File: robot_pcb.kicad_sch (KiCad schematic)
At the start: 112 parts, among them J1 Raspberry_Pi_2_3, J10 Servo_TrayRelease, J14 Motor FR, J16 19V Output, J17 Programmer, J2 Power_Bypass, J23 Motor BR, J25 ConductClaw, J26 Motor BL, J27 TOF_Front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

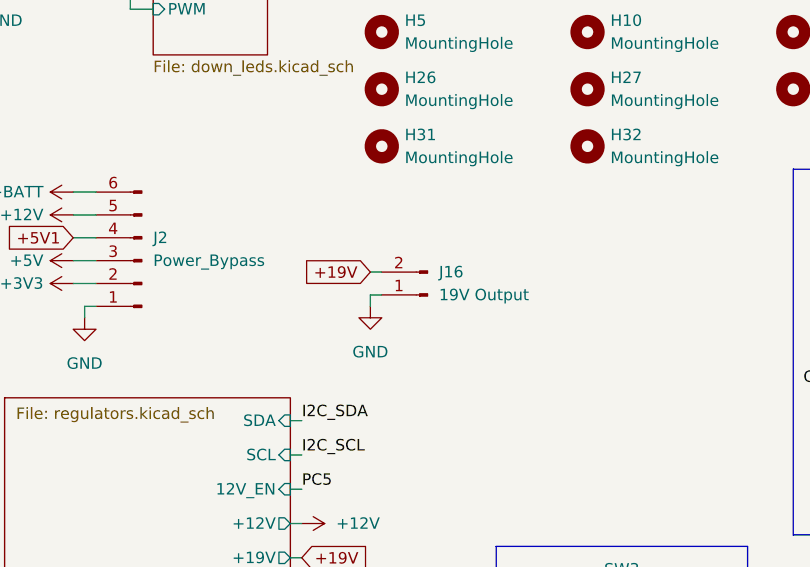
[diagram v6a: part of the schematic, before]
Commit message: Marked 19V regulator as DNP to simplify next board iteration
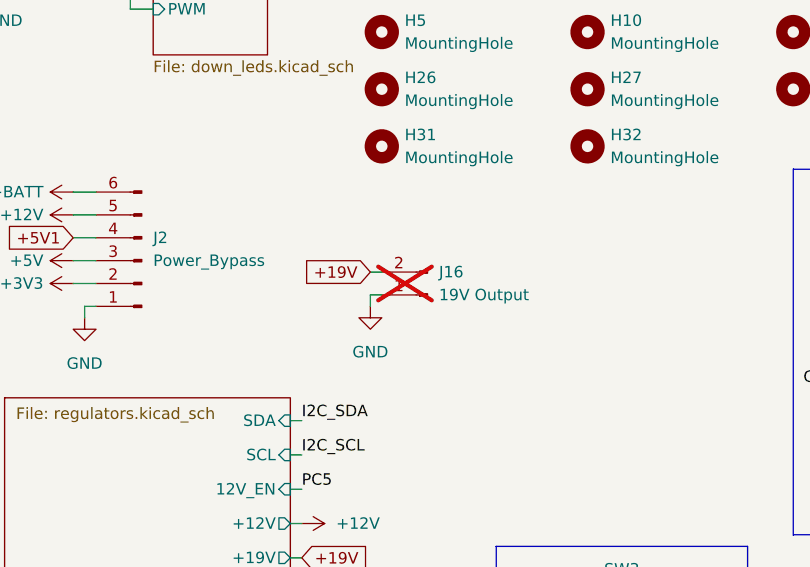
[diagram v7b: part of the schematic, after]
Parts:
- J16: now not fitted
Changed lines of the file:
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@@
 		(on_board yes)
 		(in_pos_files yes)
-		(dnp no)
+		(dnp yes)
 		(fields_autoplaced yes)
 		(property "Reference" "J16"

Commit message: switch now bigger
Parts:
- J7: LCSC C52016392 -> C541851
- SW3, SW5: footprint Button_Switch_SMD:SW_Push_1P1T_NO_CK_KMR2 -> Dry_Lettuce:SW_Push_1P1T_NO_CK_new; LCSC C51927445 -> C431539
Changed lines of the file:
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@@
 			)
 		)
-		(property "LCSC" "C52016392"
+		(property "LCSC" "C541851"
 			(at 370.84 205.74 90)
 			(hide yes)
@@
 			)
 		)
-		(property "Footprint" "Button_Switch_SMD:SW_Push_1P1T_NO_CK_KMR2"
+		(property "Footprint" "Dry_Lettuce:SW_Push_1P1T_NO_CK_new"
 			(at 143.51 154.94 0)
 			(hide yes)
@@
 			)
 		)
-		(property "Datasheet" "https://www.lcsc.com/datasheet/C51927445.pdf"
+		(property "Datasheet" ""
 			(at 143.51 154.94 0)
 			(hide yes)
@@
 			)
 		)
-		(property "LCSC" "C51927445"
+		(property "LCSC" "C431539"
 			(at 143.51 160.02 0)
 			(hide yes)
@@
 			)
 		)
-		(property "Footprint" "Button_Switch_SMD:SW_Push_1P1T_NO_CK_KMR2"
+		(property "Footprint" "Dry_Lettuce:SW_Push_1P1T_NO_CK_new"
 			(at 143.51 166.37 0)
 			(hide yes)
@@
 			)
 		)
-		(property "Datasheet" "https://www.lcsc.com/datasheet/C51927445.pdf"
+		(property "Datasheet" ""
 			(at 143.51 166.37 0)
 			(hide yes)
@@
 			)
 		)
-		(property "LCSC" "C51927445"
+		(property "LCSC" "C431539"
 			(at 143.51 171.45 0)
 			(hide yes)
